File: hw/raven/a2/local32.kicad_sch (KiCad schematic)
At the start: 93 parts, among them J301 SIMM72, J302 SIMM72, J303 SIMM72, J304 SIMM72, J305 PWM, J306 VUSB, J307 USB2Header, J308 ARGB, J309 ESSI0, J310 ESSI1, J311 DSP_JTAG, U301 CH559L, U302 XR68M752, U303 CH213K, U304 MAX3245CAI+T, U305 DSP56303, U306 AS7C31024B-xxTJ, U307 AS7C31024B-xxTJ, U308 AS7C31024B-xxTJ, U309 SN74LVC1G14DBV, U311 PCM5102A, Y301 ASE-24.000MHZ-L-C-T, Y302 ASELJ-E-22.5792MHz

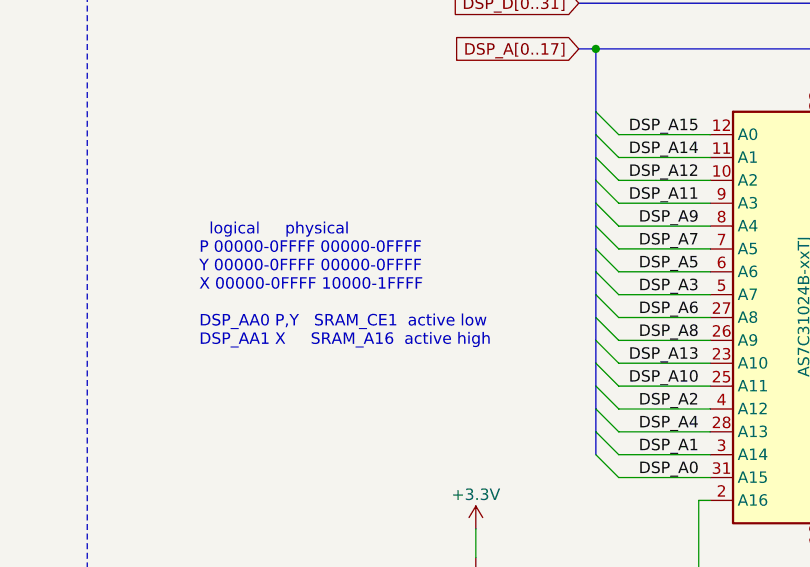
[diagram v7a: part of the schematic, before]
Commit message: A2: fixed comment about DSP ram memory map
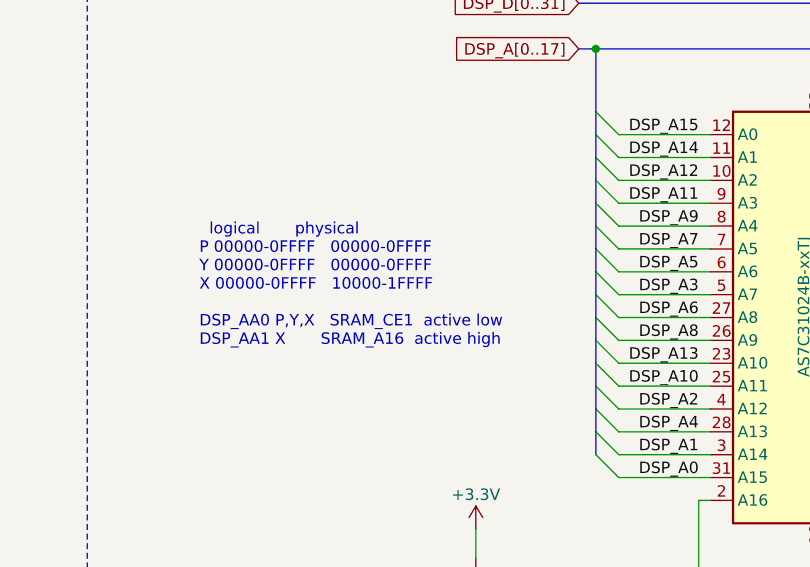
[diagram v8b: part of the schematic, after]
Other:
- note added: "logical physical P 00000-0FFFF 00000-0FFFF Y 00000-0FFFF 00000-0FFFF X 00000-0FFFF 10000-1FFFF DSP_AA0 P,Y,X SRAM_CE1 active low DSP_AA1 X SRAM_A16 active high"
- note removed: "logical physical P 00000-0FFFF 00000-0FFFF Y 00000-0FFFF 00000-0FFFF X 00000-0FFFF 10000-1FFFF DSP_AA0 P,Y SRAM_CE1 active low DSP_AA1 X SRAM_A16 active high"
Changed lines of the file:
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@@
 		)
 	)
-	(text "\n  logical     physical\nP 00000-0FFFF 00000-0FFFF\nY 00000-0FFFF 00000-0FFFF\nX 00000-0FFFF 10000-1FFFF\n\nDSP_AA0 P,Y   SRAM_CE1  active low\nDSP_AA1 X     SRAM_A16  active high\n"
+	(text "\n  logical       physical\nP 00000-0FFFF   00000-0FFFF\nY 00000-0FFFF   00000-0FFFF\nX 00000-0FFFF   10000-1FFFF\n\nDSP_AA0 P,Y,X   SRAM_CE1  active low\nDSP_AA1 X       SRAM_A16  active high\n"
 		(exclude_from_sim no)
 		(at 34.036 421.513 0)
